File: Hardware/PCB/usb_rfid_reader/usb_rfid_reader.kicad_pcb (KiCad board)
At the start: 4 copper layers, 90 x 90 mm, 35 parts, among them J1 629722000214, J2 Conn_01x08, J3 Conn_ST_STDC14, Q1 2N3904, SW1 RESET, SW2 RESET, U1 AZ1117CH2-3.3, U2 USBLC6-2SC6, U3 STM32L476RGTx

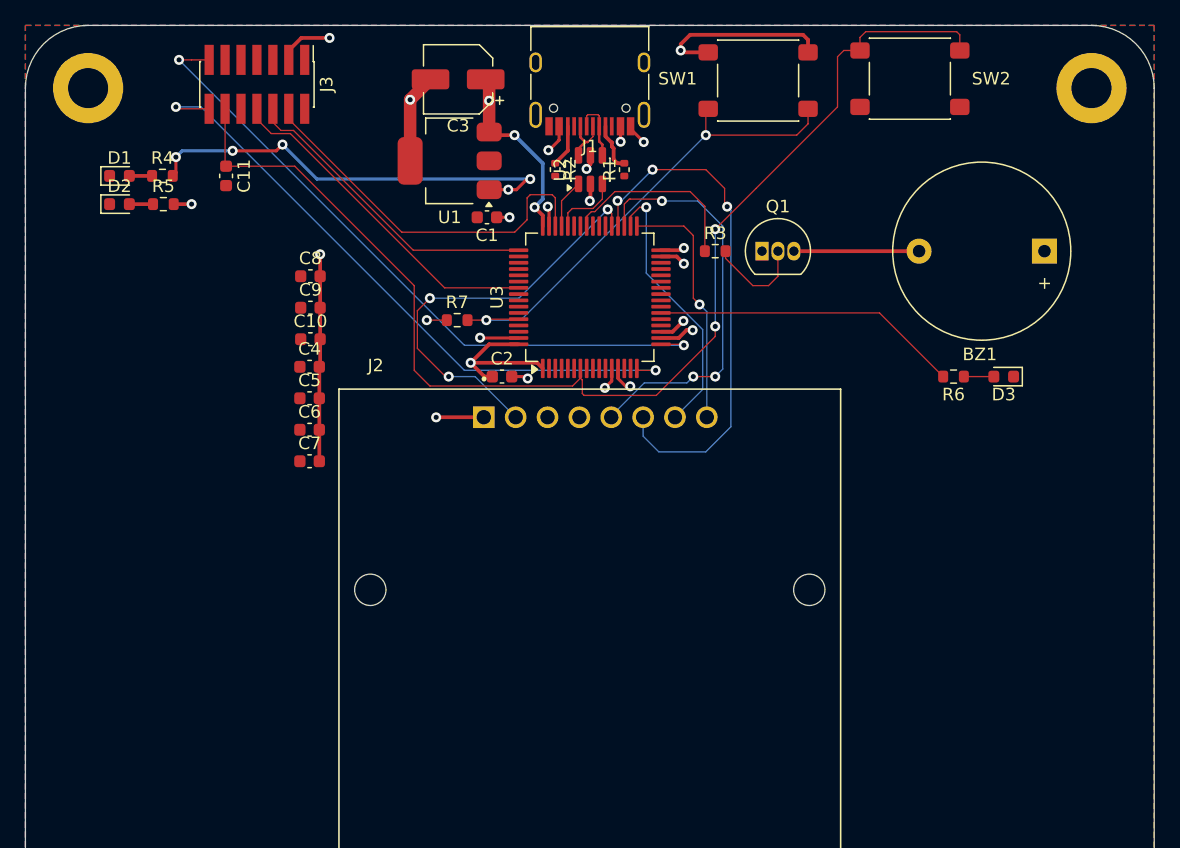
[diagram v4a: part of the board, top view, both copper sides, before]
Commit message: Ajout commentaires silkscreen PCB
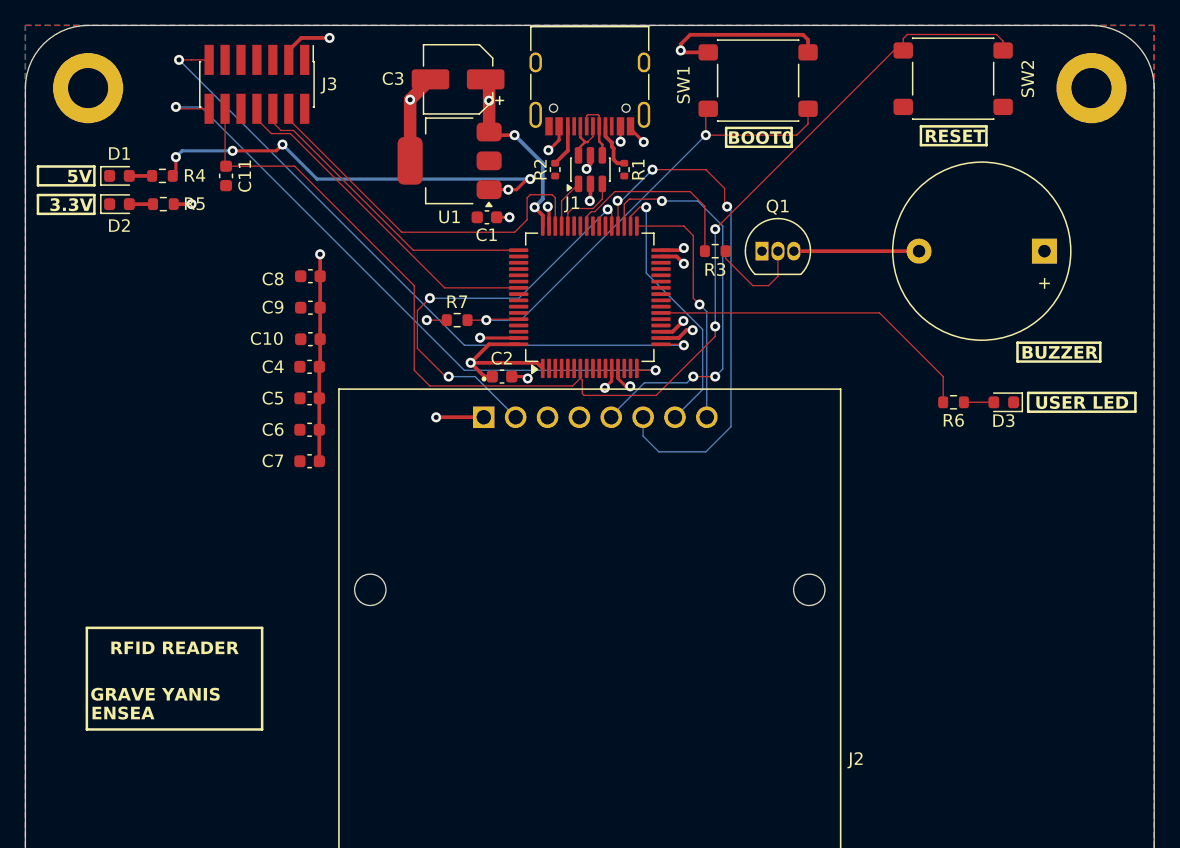
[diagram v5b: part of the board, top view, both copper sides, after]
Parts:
- SW1: value RESET -> BOOT0
- moved SW2 3.45 mm to (129.0, 49.2)
- moved D3 2.05 mm to (133.0, 75.0)
- moved R6 2.05 mm to (129.0, 75.0)
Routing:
- net /USER_LED: track 24.6 -> 26.7 mm
- net /NRST: track 97.9 -> 98.5 mm
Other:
- board text added: "3.3V"
- board text added: "5V"
- board text added: "BOOT0"
- board text added: "BUZZER"
- board text added: "ENSEA"
- board text added: "GRAVE YANIS"
- board text added: "RESET"
- board text added: "RFID READER"
- board text added: "USER LED"

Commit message: Correctifs japonais
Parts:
- moved C10 31.4 mm to (109.1, 71.5), turned to 180 degrees
- moved C8 31.1 mm to (108.7, 67.5), turned to 180 degrees
- moved C9 29.9 mm to (106.8, 60.8)
- moved C7 29.0 mm to (105.8, 72.9), turned to 180 degrees
- moved C11 20.6 mm to (84.3, 72.8), turned to 180 degrees
- moved C6 15.6 mm to (92.6, 72.8)
- moved C4 15.3 mm to (90.2, 63.4), turned to 90 degrees
- moved C5 13.9 mm to (91.2, 71.3)
- moved C2 13.9 mm to (87.5, 60.3)
- moved Q1 1.28 mm to (113.8, 61.7), turned to -90 degrees
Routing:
- net +3.3V: track 74.8 -> 54.9 mm, vias 12 -> 15
- net /NRST: track 98.5 -> 109.0 mm
- net /SWDIO: track 30.4 -> 35.8 mm
- net Net-(Q1-B): track 7.96 -> 2.98 mm
- net /SWCLK: track 24.9 -> 29.0 mm
- net /RC522_SPI2_CE_N: track 19.7 -> 23.4 mm
- net Net-(BZ1--): track 9.98 -> 13.0 mm
- net /RC522_SPI2_MISO: track 32.6 -> 35.1 mm
- net /RC522_SPI2_MOSI: track 41.3 -> 43.7 mm
- net /BOOT0: track 39.6 -> 37.9 mm
- net /USER_LED: track 26.7 -> 28.3 mm
- net /VCP_USART2_TX: track 51.2 -> 52.7 mm
- net GND: track 24.5 -> 25.7 mm, vias 10 -> 92
- net /SWO: track 27.3 -> 28.1 mm

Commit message: correctifs japonais 2
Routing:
- net GND: vias 92 -> 101
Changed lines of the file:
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@@
 	)
 	(gr_rect
-		(start 59.9 93.035)
-		(end 73.875 101.135)
+		(start 60.075 90)
+		(end 75.1 98.1)
 		(stroke
 			(width 0.2)
@@
 	)
 	(gr_text "GRAVE YANIS"
-		(at 60.175 98.95 0)
+		(at 60.45 95.915 0)
 		(layer "F.SilkS")
 		(effects
@@
 	)
 	(gr_text "ENSEA\n"
-		(at 60.225 100.45 0)
+		(at 60.5 97.415 0)
 		(layer "F.SilkS")
 		(effects
@@
 	)
 	(gr_text "RFID READER"
-		(at 61.725 95.25 0)
+		(at 61.725 92.215 0)
 		(layer "F.SilkS")
 		(effects
@@
 	)
 	(via
+		(at 140 55)
+		(size 0.8)
+		(drill 0.4)
+		(layers "F.Cu" "B.Cu")
+		(free yes)
+		(net 3)
+	)
+	(via
 		(at 60 75)
 		(size 0.8)
@@
 	)
 	(via
+		(at 75 130)
+		(size 0.8)
+		(drill 0.4)
+		(layers "F.Cu" "B.Cu")
+		(free yes)
+		(net 3)
+	)
+	(via
 		(at 60 85)
 		(size 0.8)
@@
 	)
 	(via
+		(at 65 130)
+		(size 0.8)
+		(drill 0.4)
+		(layers "F.Cu" "B.Cu")
+		(free yes)
+		(net 3)
+	)
+	(via
+		(at 125 130)
+		(size 0.8)
+		(drill 0.4)
+		(layers "F.Cu" "B.Cu")
+		(free yes)
+		(net 3)
+	)
+	(via
 		(at 140 90)
 		(size 0.8)
@@
 	)
 	(via
+		(at 70 130)
+		(size 0.8)
+		(drill 0.4)
+		(layers "F.Cu" "B.Cu")
+		(free yes)
+		(net 3)
+	)
+	(via
 		(at 130 120)
 		(size 0.8)
@@
 	)
 	(via
+		(at 135 130)
+		(size 0.8)
+		(drill 0.4)
+		(layers "F.Cu" "B.Cu")
+		(free yes)
+		(net 3)
+	)
+	(via
 		(at 135 120)
 		(size 0.8)
@@
 	)
 	(via
+		(at 130 130)
+		(size 0.8)
+		(drill 0.4)
+		(layers "F.Cu" "B.Cu")
+		(free yes)
+		(net 3)
+	)
+	(via
 		(at 140 100)
 		(size 0.8)
@@
 	)
 	(via
+		(at 140 60)
+		(size 0.8)
+		(drill 0.4)
+		(layers "F.Cu" "B.Cu")
+		(free yes)
+		(net 3)
+	)
+	(via
 		(at 75 70)
 		(size 0.8)
@@
 		(net 3)
 	)
+	(via
+		(at 140 65)
+		(size 0.8)
+		(drill 0.4)
+		(layers "F.Cu" "B.Cu")
+		(free yes)
+		(net 3)
+	)

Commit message: correctifs japonais V3
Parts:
- moved C2 8.18 mm to (94.4, 56.0), turned to -90 degrees
- moved C11 3.19 mm to (87.5, 73.0)
- moved J3 1.30 mm to (73.5, 51.0)
- moved C6 1.04 mm to (93.7, 72.8)
- moved BZ1 1.03 mm to (136.0, 64.0)
- moved SW2 0.75 mm to (129.0, 50.0)
- moved SW1 0.60 mm to (113.4, 50.0)
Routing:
- net +3.3V: track 54.9 -> 38.9 mm
- net /NRST: track 109.0 -> 97.4 mm, vias 2 -> 3
- net +5V: track 40.4 -> 30.0 mm, vias 9 -> 7
- net /VCP_USART2_TX: track 52.7 -> 47.8 mm
- net /VCP_USART2_RX: track 54.3 -> 50.8 mm
- net GND: track 25.7 -> 24.0 mm, vias 101 -> 156
- net /SWCLK: track 29.0 -> 27.4 mm
- net /SWO: track 28.1 -> 26.7 mm
- net /SWDIO: track 35.8 -> 34.5 mm
- net /RC522_RST: track 33.3 -> 32.3 mm
- net /RC522_SPI2_MOSI: track 43.7 -> 42.8 mm
- net unconnected-(U3-PC9-Pad40): track 0.67 -> 0.00 mm
- net Net-(BZ1--): track 13.0 -> 12.3 mm
- net /BOOT0: track 37.9 -> 37.3 mm
